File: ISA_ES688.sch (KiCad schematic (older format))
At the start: 105 parts, among them J1 LINE IN, J10 Vol. Btns, J11 ISA BUS, J2 MIC, J3 Joystick/MIDI, J5 Wavetable, J7 SPKR OUT, J8 LINE OUT, U1 L78L05, U2 74LS138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

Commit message: Add NE558 symbol
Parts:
- removed C17: 100nF, Capacitor_THT:C_Disc_D6.0mm_W2.5mm_P5.00mm, symbol Device:C_Small
- removed J10: Vol. Btns, Connector_PinHeader_2.54mm:PinHeader_2x03_P2.54mm_Vertical, symbol Connector_Generic:Conn_02x03_Odd_Even
- removed JP1: Intl. ROM 1, Jumper:SolderJumper-3_P1.3mm_Open_RoundedPad1.0x1.5mm_NumberLabels, symbol Jumper:Jumper_3_Open
- removed JP2: Intl. ROM 2, Jumper:SolderJumper-3_P1.3mm_Open_RoundedPad1.0x1.5mm_NumberLabels, symbol Jumper:Jumper_3_Open
- removed R14, R15, R16, R17: 1k, Resistor_THT:R_Axial_DIN0207_L6.3mm_D2.5mm_P7.62mm_Horizontal, symbol Device:R_Small
- removed U2: 74LS138, Package_DIP:DIP-16_W7.62mm_LongPads, symbol 74xx:74LS138
- removed U3: ES1868F, Package_QFP:LQFP-14x20mm_P0.5mm, symbol custom_components:ES1868F
- removed U4: 93LC66, Package_DIP:DIP-8_W7.62mm_LongPads, symbol Memory_EEPROM:93CxxC
- added U?: ES688F, symbol custom_components:ES688F
- added U?: 74LS245, symbol 74xx:74LS245
- added U?: 74LS244, symbol 74xx:74LS244
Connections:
- wire segments 557 -> 467
- no-connect marks 46 -> 39
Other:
- note removed: "1-2 External ROM\n2-3 Internal ROM"

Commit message: Begin changing the schematics
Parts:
- removed J8: LINE OUT, Connector_PinHeader_2.54mm:PinHeader_1x03_P2.54mm_Horizontal, symbol Connector_Generic:Conn_01x03
- removed R7: 10k, Resistor_THT:R_Axial_DIN0207_L6.3mm_D2.5mm_P7.62mm_Horizontal, symbol Device:R_Small
- added J8: MIC, Connector_PinHeader_2.54mm:PinHeader_1x02_P2.54mm_Horizontal, symbol Connector:Conn_01x02_Male
- added U?: NE558, symbol custom_components:NE558
- J2: value MIC -> LINE OUT
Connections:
- wire segments 467 -> 452
- no-connect marks 39 -> 22
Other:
- moved on the sheet: C36, C37, J2
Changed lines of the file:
@@
 	12950 7400 14300 7400
 Wire Wire Line
-	14300 8500 14300 7400
-Wire Wire Line
-	14750 8500 14300 8500
+	14750 8200 14300 8200
 Wire Wire Line
 	12950 7500 14200 7500
 Wire Wire Line
-	14200 8400 14200 7500
-Wire Wire Line
-	14750 8400 14200 8400
-Wire Wire Line
-	14950 8500 15500 8500
+	14750 8500 14200 8500
 $Comp
 L Device:C_Small C37
 U 1 1 60B9D219
+P 14850 8200
+F 0 "C37" V 14900 8300 50  0000 L CNN
+F 1 "10uF" V 14900 7900 50  0000 L CNN
+F 2 "Capacitor_THT:C_Disc_D6.0mm_W2.5mm_P5.00mm" H 14850 8200 50  0001 C CNN
+F 3 "~" H 14850 8200 50  0001 C CNN
+	1    14850 8200
+	0    -1   1    0
+$EndComp
+$Comp
+L Device:C_Small C36
+U 1 1 60B9B492
 P 14850 8500
-F 0 "C37" V 14900 8600 50  0000 L CNN
+F 0 "C36" V 14900 8600 50  0000 L CNN
 F 1 "10uF" V 14900 8200 50  0000 L CNN
 F 2 "Capacitor_THT:C_Disc_D6.0mm_W2.5mm_P5.00mm" H 14850 8500 50  0001 C CNN
 F 3 "~" H 14850 8500 50  0001 C CNN
 	1    14850 8500
-	0    -1   1    0
-$EndComp
-$Comp
-L Device:C_Small C36
-U 1 1 60B9B492
-P 14850 8400
-F 0 "C36" V 14900 8500 50  0000 L CNN
-F 1 "10uF" V 14900 8100 50  0000 L CNN
-F 2 "Capacitor_THT:C_Disc_D6.0mm_W2.5mm_P5.00mm" H 14850 8400 50  0001 C CNN
-F 3 "~" H 14850 8400 50  0001 C CNN
-	1    14850 8400
 	0    -1   1    0
 $EndComp
@@
 	1    0    0    -1
 $EndComp
-Text Label 13400 8850 2    50   ~ 0
-MSI
-Text Label 13400 8950 2    50   ~ 0
-MSO
-Text Label 13400 9050 2    50   ~ 0
-MSD
-Text Label 13400 9150 2    50   ~ 0
-MCLK
-Text Label 13400 9250 2    50   ~ 0
-~RSTB
-Wire Wire Line
-	12950 9250 13400 9250
-Wire Wire Line
-	12950 9150 13400 9150
-Wire Wire Line
-	12950 9050 13400 9050
-Wire Wire Line
-	12950 8950 13400 8950
-Wire Wire Line
-	12950 8850 13400 8850
-Wire Wire Line
-	13100 9850 12950 9850
-Wire Wire Line
-	13450 9850 13450 9900
-Wire Wire Line
-	13300 9850 13450 9850
-$Comp
-L power:GND #PWR0125
-U 1 1 60C150B5
-P 13450 9900
-F 0 "#PWR0125" H 13450 9650 50  0001 C CNN
-F 1 "GND" H 13455 9727 50  0000 C CNN
-F 2 "" H 13450 9900 50  0001 C CNN
-F 3 "" H 13450 9900 50  0001 C CNN
-	1    13450 9900
-	1    0    0    -1
-$EndComp
-$Comp
-L Device:R_Small R7
-U 1 1 60C11710
-P 13200 9850
-F 0 "R7" V 13300 9800 50  0000 L CNN
-F 1 "10k" V 13100 9750 50  0000 L CNN
-F 2 "Resistor_THT:R_Axial_DIN0207_L6.3mm_D2.5mm_P7.62mm_Horizontal" H 13200 9850 50  0001 C CNN
-F 3 "~" H 13200 9850 50  0001 C CNN
-	1    13200 9850
-	0    -1   -1   0
-$EndComp
-NoConn ~ 12950 9750
-NoConn ~ 12950 9650
-NoConn ~ 12950 9550
-NoConn ~ 12950 9450
-NoConn ~ 12950 9350
-NoConn ~ 12950 8750
-NoConn ~ 12950 8650
-NoConn ~ 12950 8550
-NoConn ~ 12950 8450
-NoConn ~ 12950 8350
-NoConn ~ 12950 8250
-NoConn ~ 12950 8150
-NoConn ~ 12950 8050
-NoConn ~ 12950 7950
-NoConn ~ 12950 7850
 Text Label 13850 7500 2    50   ~ 0
 AOUTR
@@
 Connection ~ 15200 6150
 Wire Wire Line
-	15200 6150 15200 6250
-Wire Wire Line
 	13750 6150 15200 6150
 Wire Wire Line
@@
 	0    -1   -1   0
 $EndComp
-NoConn ~ 12950 5550
-NoConn ~ 12950 5450
 Text Label 14200 5200 2    50   ~ 0
 AUXBR
@@
 	1    0    0    -1
 $EndComp
-Wire Wire Line
-	12400 4200 12500 4200
-Wire Wire Line
-	12400 4300 12400 4200
-Wire Wire Line
-	12500 4200 12500 4300
 Text Label 7700 5700 2    50   ~ 0
 ~RSTB
@@
 L my_components:JACK_TRS_3PINS J2
 U 1 1 62C8E737
-P 16250 6250
-F 0 "J2" H 15872 6209 50  0000 R CNN
-F 1 "MIC" H 15872 6300 50  0000 R CNN
-F 2 "My_Components:Conn_Audio_3.5mm_Stereo_SJ1-352XNG" H 15872 6346 50  0001 R CNN
-F 3 "" H 16400 6400 50  0000 C CNN
-	1    16250 6250
-	-1   0    0    1
-$EndComp
-Wire Wire Line
-	15650 6250 15650 6450
-Wire Wire Line
-	15650 6450 15800 6450
-Wire Wire Line
-	15200 6250 15650 6250
+P 15950 8400
+F 0 "J2" H 15572 8359 50  0000 R CNN
+F 1 "LINE OUT" H 15572 8450 50  0000 R CNN
+F 2 "My_Components:Conn_Audio_3.5mm_Stereo_SJ1-352XNG" H 15572 8496 50  0001 R CNN
+F 3 "" H 16100 8550 50  0000 C CNN
+	1    15950 8400
+	-1   0    0    -1
+$EndComp
 Wire Wire Line
 	15200 6150 15800 6150
@@
 Text Label 13500 4650 0    50   ~ 0
 VDDA
-$Comp
-L Connector_Generic:Conn_01x03 J8
-U 1 1 633797AC
-P 15700 8500
-F 0 "J8" H 15780 8542 50  0000 L CNN
-F 1 "LINE OUT" H 15780 8451 50  0000 L CNN
-F 2 "Connector_PinHeader_2.54mm:PinHeader_1x03_P2.54mm_Horizontal" H 15700 8500 50  0001 C CNN
-F 3 "~" H 15700 8500 50  0001 C CNN
-	1    15700 8500
-	1    0    0    -1
-$EndComp
-Wire Wire Line
-	14950 8400 15500 8400
+Wire Wire Line
+	14950 8500 15500 8500
 Text Label 17550 4000 0    50   ~ 0
 Filtered_12V
@@
 	1    0    0    -1
 $EndComp
+$Comp
+L custom_components:NE558 U?
+U 1 1 60D93AFC
+P 2700 2900
+F 0 "U?" H 2700 3903 60  0000 C CNN
+F 1 "NE558" H 2700 3797 60  0000 C CNN
+F 2 "" H 3200 3100 60  0000 C CNN
+F 3 "" H 3200 3100 60  0000 C CNN
+	1    2700 2900
+	1    0    0    -1
+$EndComp
+Wire Wire Line
+	14300 8200 14300 7400
+Wire Wire Line
+	14950 8200 15500 8200
+Wire Wire Line
+	14200 7500 14200 8500
+$Comp
+L Connector:Conn_01x02_Male J8
+U 1 1 61118C7C
+P 16000 6150
+F 0 "J8" H 15972 6032 50  0000 R CNN
+F 1 "MIC" H 15972 6123 50  0000 R CNN
+F 2 "Connector_PinHeader_2.54mm:PinHeader_1x02_P2.54mm_Horizontal" H 16000 6150 50  0001 C CNN
+F 3 "~" H 16000 6150 50  0001 C CNN
+	1    16000 6150
+	-1   0    0    1
+$EndComp
 $EndSCHEMATC

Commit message: Remove some unused components
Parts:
- removed J5: Wavetable, Connector_PinHeader_2.54mm:PinHeader_2x13_P2.54mm_Vertical, symbol Connector_Generic:Conn_02x13_Odd_Even
- removed R18: 22k, Resistor_THT:R_Axial_DIN0207_L6.3mm_D2.5mm_P7.62mm_Horizontal, symbol Device:R_Small
- U?: footprint (none) -> Package_QFP:LQFP-14x20mm_P0.5mm
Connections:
- net labels removed: MCLK, MSD, ~RSTB
- wire segments 452 -> 454
- no-connect marks 22 -> 19
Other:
- moved on the sheet: C46, U?

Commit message: Complete more schematic
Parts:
- removed C29, C30: 220nF, Capacitor_THT:C_Disc_D6.0mm_W2.5mm_P5.00mm, symbol Device:C_Small
- removed JP3: ~DRQ2~ Jumper, Jumper:SolderJumper-2_P1.3mm_Open_RoundedPad1.0x1.5mm, symbol Device:Jumper_NO_Small
- removed JP4: ~DACK2~ Jumper, Jumper:SolderJumper-2_P1.3mm_Open_RoundedPad1.0x1.5mm, symbol Device:Jumper_NO_Small
- removed JP5: IRQ3 Jumper, Jumper:SolderJumper-2_P1.3mm_Open_RoundedPad1.0x1.5mm, symbol Device:Jumper_NO_Small
- removed JP6: IRQ4 Jumper, Jumper:SolderJumper-2_P1.3mm_Open_RoundedPad1.0x1.5mm, symbol Device:Jumper_NO_Small
- added J?: Interrupt Select, symbol Connector_Generic:Conn_02x02_Odd_Even
- added J?: Address Select, symbol Connector_Generic:Conn_02x02_Odd_Even
- added J?: DMA Select, symbol Connector_Generic:Conn_02x02_Odd_Even
- added JP?: Emulation Mode, symbol Device:Jumper_NO_Small
- added JP?: ~DRQ2~ Jumper, symbol Device:Jumper_NO_Small
- added JP?: ~DACK2~ Jumper, symbol Device:Jumper_NO_Small
- added R?: 10k, Resistor_THT:R_Axial_DIN0207_L6.3mm_D2.5mm_P7.62mm_Horizontal, symbol Device:R_Small
- added RN?: 10k, Resistor_THT:R_Array_SIP9, symbol Device:R_Network08
- C14: value 47uF -> 10uF
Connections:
- net labels added: ES-D0, ES-D1, ES-D2, ES-D3, ES-D4, ES-D5, ES-D6, ES-D7, MIDI_IN, MIDI_OUT, MUS_L, MUS_R, ~FMENB245, ~JOY_R, ~JOY_W
- net labels removed: AUXBL, AUXBR
- wire segments 454 -> 528
- no-connect marks 19 -> 24
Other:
- note added: "Default to\nSound Blaster PRO"
- moved on the sheet: C10, C11, C12, C13, C14, C15, C16, C27, C28, C33, C34, C35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

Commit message: Cleanup for joystick part
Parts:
- removed C18, C19, C20, C21, C23, C24, C25, C26: 10nF, Capacitor_THT:C_Disc_D6.0mm_W2.5mm_P5.00mm, symbol Device:C_Small
- removed R10, R11, R3, R4, R5, R6, R8, R9: 2.2k, Resistor_THT:R_Axial_DIN0207_L6.3mm_D2.5mm_P7.62mm_Horizontal, symbol Device:R_Small
- removed R34, R35, R36, R37: 1M, Resistor_THT:R_Axial_DIN0207_L6.3mm_D2.5mm_P7.62mm_Horizontal, symbol Device:R_Small
- R12, R13: value 2.2k -> 30
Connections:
- net MSI is gone; now on net MIDI_IN: R13.2
- net MSO is gone; now on net MIDI_OUT: R12.2
- net GND: now also U?.10 (GND), U?.12 (GND)
- net VCC: now also U?.20 (VCC), U?.5 (VCC)
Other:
- moved on the sheet: C22, C42, J3, L1, L2, R12, R13, U7C, U?

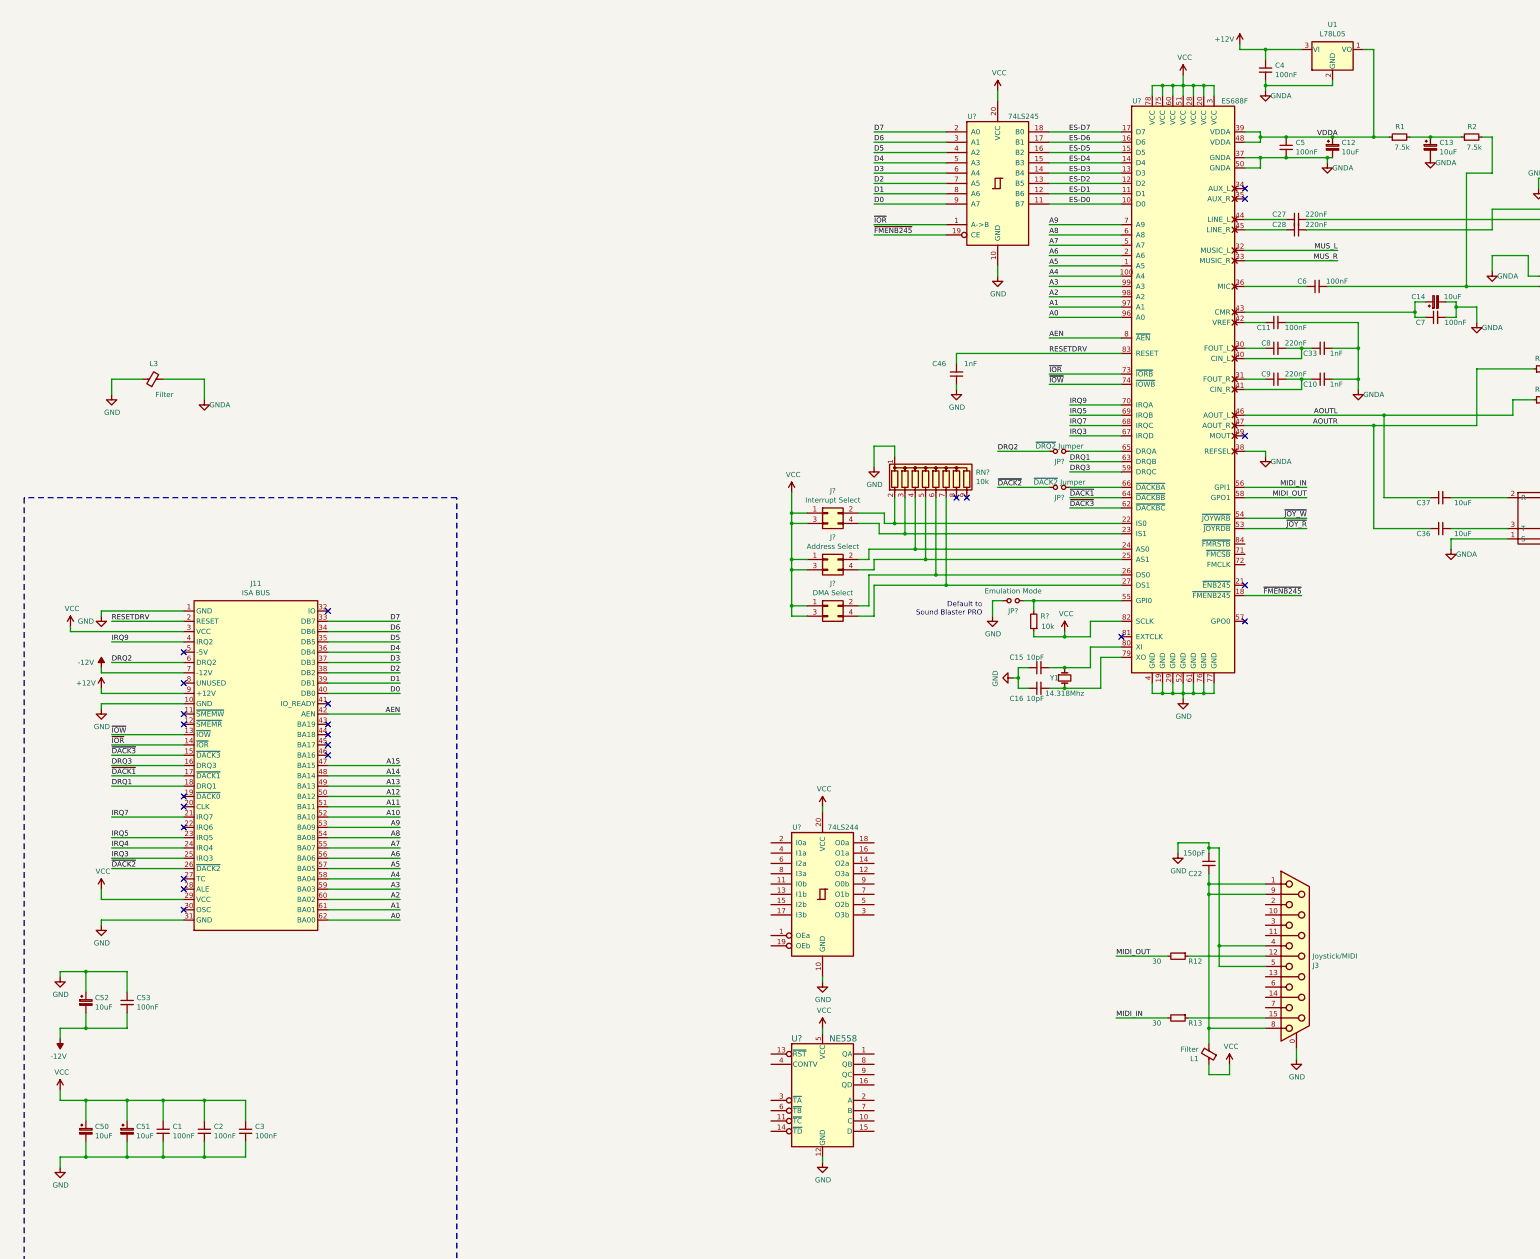
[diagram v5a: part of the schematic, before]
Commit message: More joystick schematics
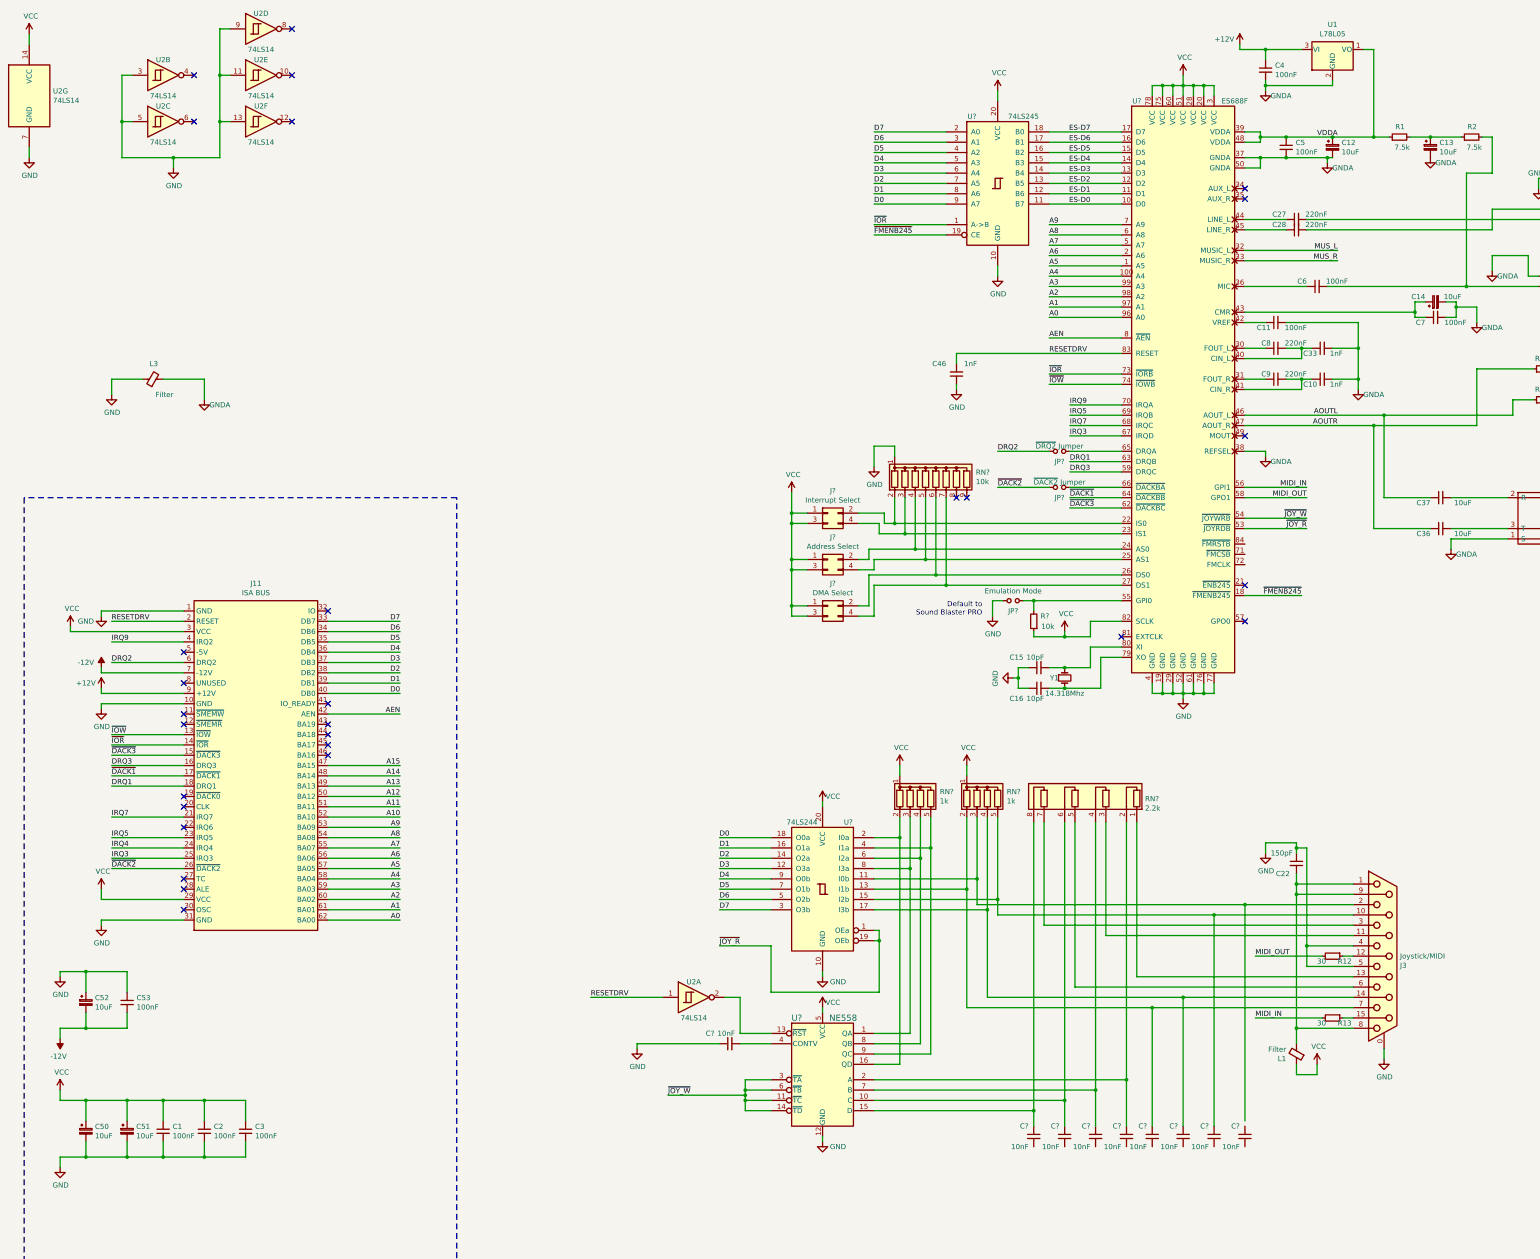
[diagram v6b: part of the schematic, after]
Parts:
- added C?: 10nF, Capacitor_THT:C_Disc_D3.8mm_W2.6mm_P2.50mm, symbol Device:C_Small
- added C? (x8): 10nF, Capacitor_THT:C_Disc_D6.0mm_W2.5mm_P5.00mm, symbol Device:C_Small
- added RN? (x2): 1k, Resistor_THT:R_Array_SIP5, symbol Device:R_Network04
- added RN?: 2.2k, Resistor_THT:R_Array_SIP8, symbol Device:R_Pack04_SIP
- added U2: 74LS14, symbol 74xx:74LS14
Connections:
- net D0: now also U?.18 (O0a)
- net D1: now also U?.16 (O1a)
- net D2: now also U?.14 (O2a)
- net D3: now also U?.12 (O3a)
- net D4: now also U?.9 (O0b)
- net D5: now also U?.7 (O1b)
- net D6: now also U?.5 (O2b)
- net D7: now also U?.3 (O3b)
- net GND: now also C?.1, U2.11, U2.13, U2.3, U2.5, U2.7 (GND), U2.9
- net RESETDRV: now also U2.1
- net VCC: now also RN?.1 (common), RN?.1 (common), U2.14 (VCC)
- net ~JOY_R: now also U?.1 (OEa), U?.19 (OEb)
- net ~JOY_W: now also U?.11 (~TC), U?.14 (~TD), U?.3 (~TA), U?.6 (~TB)
- net at U?.11 (I0b): now also J3.2, RN?.3 (R2)
- net at U?.13 (I1b): now also J3.7, C?.1, RN?.2 (R1)
- net at U?.15 (I2b): now also J3.10 (P10), C?.1, RN?.5 (R4)
- net at U?.17 (I3b): now also J3.14 (P14), C?.1, RN?.4 (R3)
- net at U?.2 (I0a): now also U?.16 (QD), RN?.2 (R1)
- net at U?.4 (I1a): now also U?.9 (QC), RN?.5 (R4)
- net at U?.6 (I2a): now also U?.8 (QB), RN?.4 (R3)
- net at U?.8 (I3a): now also U?.1 (QA), RN?.3 (R2)
- net at U?.10 (C): now also C?.1, RN?.6 (R3.2)
- net at U?.13 (~RST): now also U2.2
- net at U?.15 (D): now also C?.1, RN?.8 (R4.2)
- net at U?.2 (A): now also C?.1, RN?.2 (R1.2)
- net at U?.4 (CONTV): now also C?.2
- net at U?.7 (B): now also C?.1, RN?.4 (R2.2)
- net at J3.11 (P111): now also RN?.3 (R2.1)
- net at J3.13 (P13): now also RN?.1 (R1.1)
- net at J3.3: now also RN?.7 (R4.1)
- net at J3.6: now also RN?.5 (R3.1)
- no-connect marks 24 -> 29
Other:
- moved on the sheet: C22, J3, L1, R12, R13, U?
